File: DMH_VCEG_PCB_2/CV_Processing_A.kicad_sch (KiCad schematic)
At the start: 58 parts, among them J26 Conn_01x10_PinHeader, Q27 BC558, Q28 BC558, Q29 BC548, Q30 BC548, Q31 BC548, Q32 BC548, U18 TL074, U19 TL074, U20 TL074

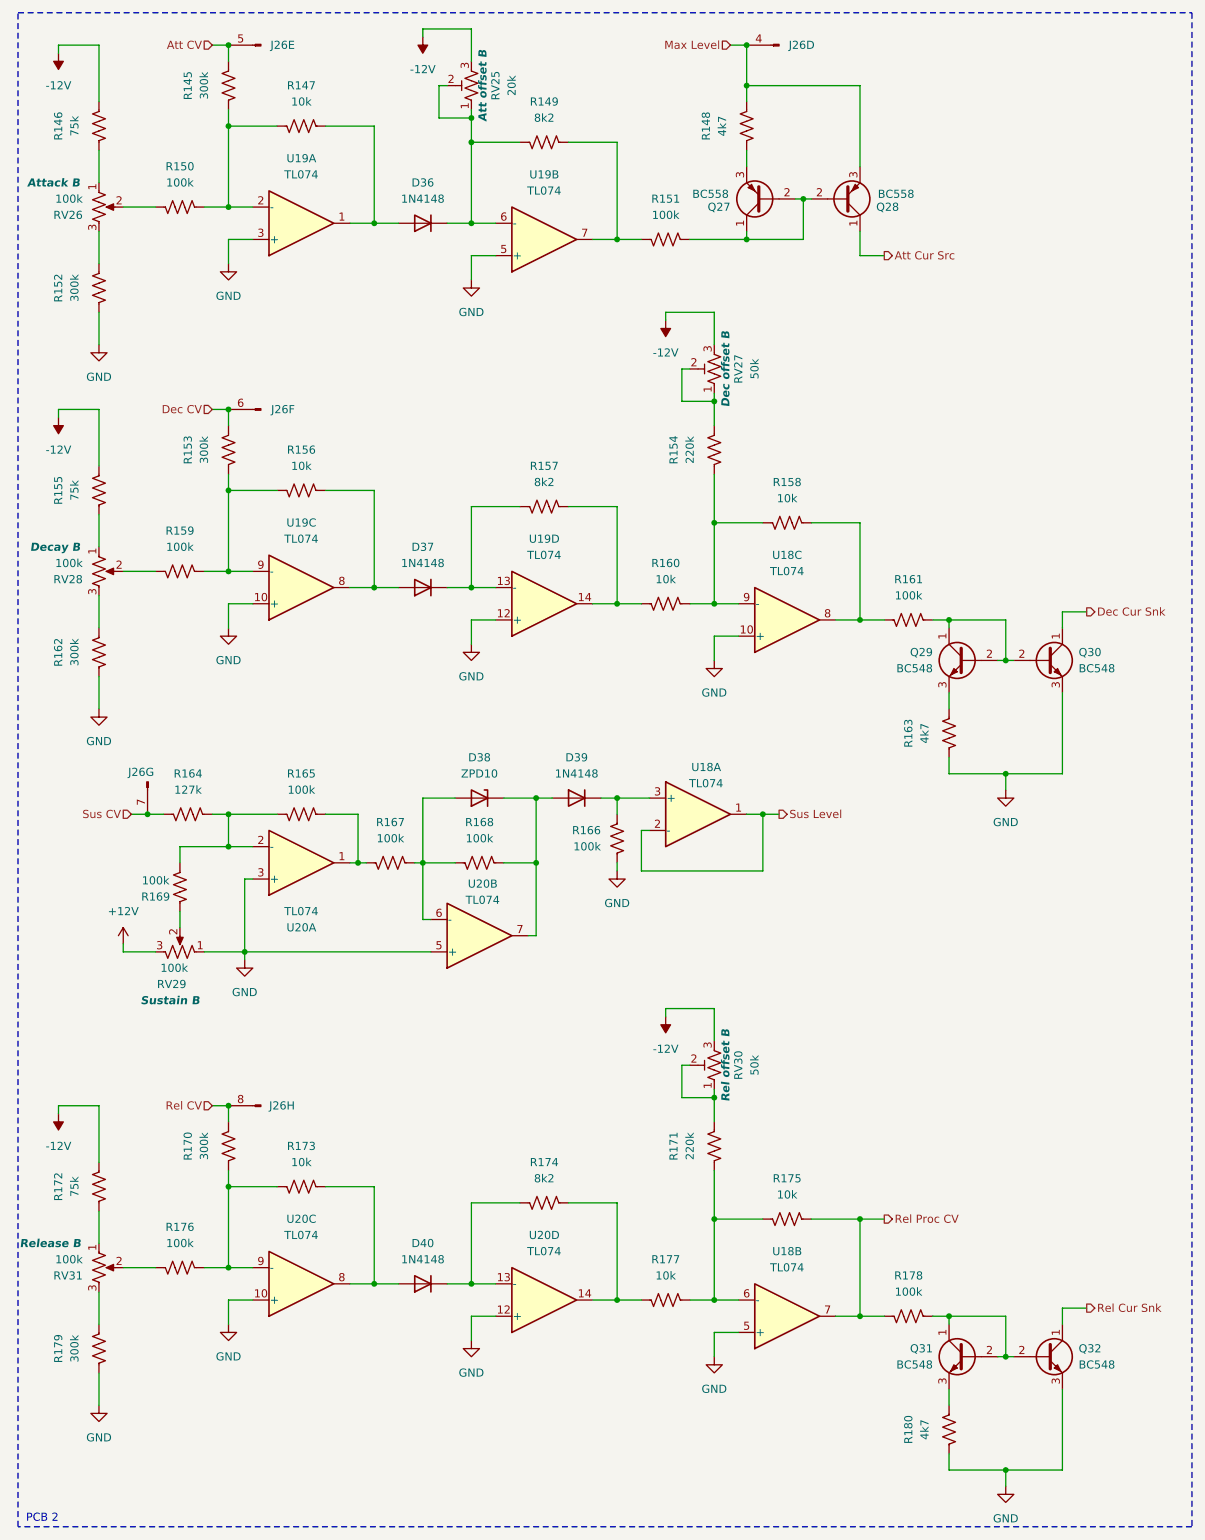
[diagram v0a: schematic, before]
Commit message: Synced PCB 2 project with PCB 1
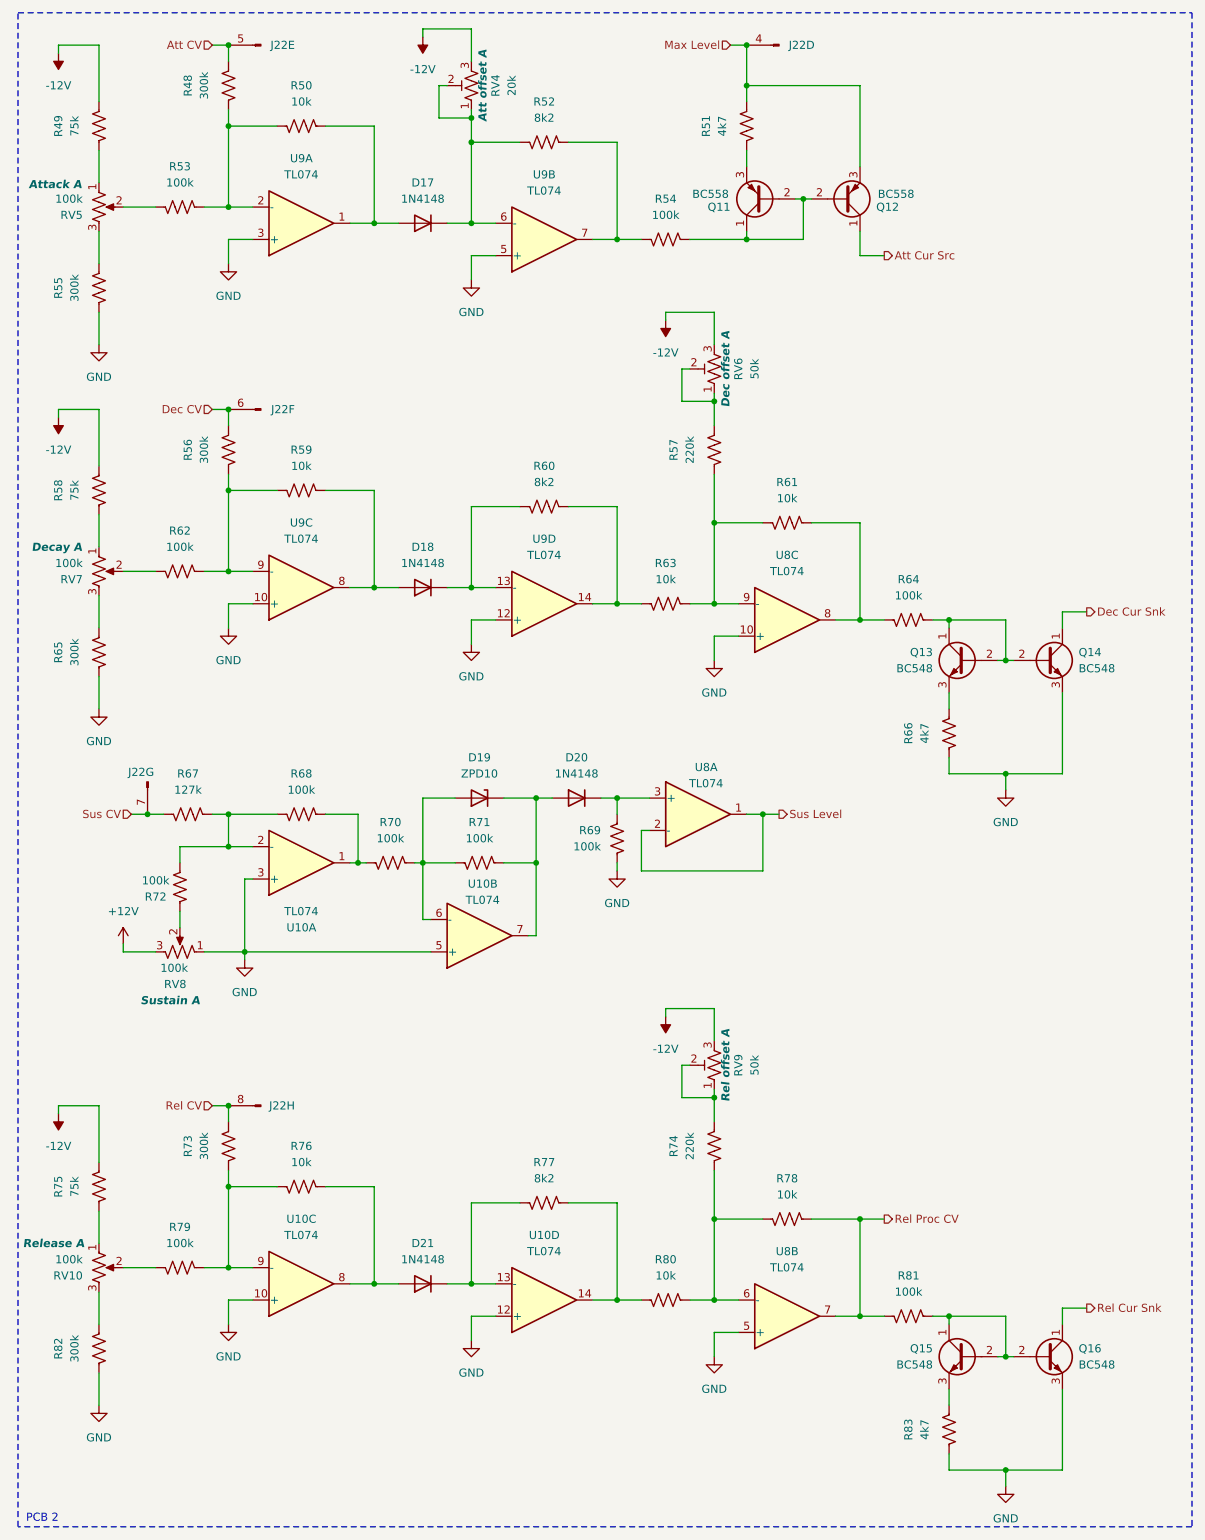
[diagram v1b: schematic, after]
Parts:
- removed D36, D37, D39, D40: 1N4148, Diode_THT:D_DO-35_SOD27_P7.62mm_Horizontal, symbol Diode:1N4148
- removed D38: ZPD10, Diode_THT:D_DO-35_SOD27_P7.62mm_Horizontal, symbol Diode:ZPDxx
- removed J26: Conn_01x10_PinHeader, Connector_PinHeader_2.54mm:PinHeader_1x10_P2.54mm_Vertical, symbol SynthStuff:Conn_01x10_PinHeader
- removed Q27, Q28: BC558, Package_TO_SOT_THT:TO-92L_Inline_Wide, symbol Transistor_BJT:BC558
- removed Q29, Q30, Q31, Q32: BC548, Package_TO_SOT_THT:TO-92L_Inline_Wide, symbol Transistor_BJT:BC548
- removed R145, R152, R153, R162, R170, R179: 300k, Resistor_THT:R_Axial_DIN0207_L6.3mm_D2.5mm_P7.62mm_Horizontal, symbol Device:R_US
- removed R146, R155, R172: 75k, Resistor_THT:R_Axial_DIN0207_L6.3mm_D2.5mm_P7.62mm_Horizontal, symbol Device:R_US
- removed R147, R156, R158, R160, R173, R175, R177: 10k, Resistor_THT:R_Axial_DIN0207_L6.3mm_D2.5mm_P7.62mm_Horizontal, symbol Device:R_US
- removed R148, R163, R180: 4k7, Resistor_THT:R_Axial_DIN0207_L6.3mm_D2.5mm_P7.62mm_Horizontal, symbol Device:R_US
- removed R149, R157, R174: 8k2, Resistor_THT:R_Axial_DIN0207_L6.3mm_D2.5mm_P7.62mm_Horizontal, symbol Device:R_US
- removed R150, R151, R159, R161, R165, R166, R167, R168, R169, R176, R178: 100k, Resistor_THT:R_Axial_DIN0207_L6.3mm_D2.5mm_P7.62mm_Horizontal, symbol Device:R_US
- removed R154, R171: 220k, Resistor_THT:R_Axial_DIN0207_L6.3mm_D2.5mm_P7.62mm_Horizontal, symbol Device:R_US
- removed R164: 127k, Resistor_THT:R_Axial_DIN0207_L6.3mm_D2.5mm_P7.62mm_Horizontal, symbol Device:R_US
- removed RV25: 20k, Potentiometer_THT:Potentiometer_Bourns_3296X_Horizontal, symbol Device:R_Potentiometer_Trim_US
- removed RV26, RV28, RV29, RV31: 100k, SynthStuff:Potentiometer_Alpha_RD901F-40-00D_Single_Vertical, symbol Device:R_Potentiometer_US
- removed RV27, RV30: 50k, Potentiometer_THT:Potentiometer_Bourns_3296X_Horizontal, symbol Device:R_Potentiometer_Trim_US
- removed U18, U19, U20: TL074, Package_DIP:DIP-14_W7.62mm_Socket, symbol Amplifier_Operational:TL074
- added D17, D18, D20, D21: 1N4148, Diode_THT:D_DO-35_SOD27_P7.62mm_Horizontal, symbol Diode:1N4148
- added D19: ZPD10, Diode_THT:D_DO-35_SOD27_P7.62mm_Horizontal, symbol Diode:ZPDxx
- added J22: Conn_01x10_PinHeader, Connector_PinSocket_2.54mm:PinSocket_1x10_P2.54mm_Vertical, symbol SynthStuff:Conn_01x10_PinHeader
- added Q11, Q12: BC558, Package_TO_SOT_THT:TO-92L_Inline_Wide, symbol Transistor_BJT:BC558
- added Q13, Q14, Q15, Q16: BC548, Package_TO_SOT_THT:TO-92L_Inline_Wide, symbol Transistor_BJT:BC548
- added R48, R55, R56, R65, R73, R82: 300k, Resistor_THT:R_Axial_DIN0207_L6.3mm_D2.5mm_P7.62mm_Horizontal, symbol Device:R_US
- added R49, R58, R75: 75k, Resistor_THT:R_Axial_DIN0207_L6.3mm_D2.5mm_P7.62mm_Horizontal, symbol Device:R_US
- added R50, R59, R61, R63, R76, R78, R80: 10k, Resistor_THT:R_Axial_DIN0207_L6.3mm_D2.5mm_P7.62mm_Horizontal, symbol Device:R_US
- added R51, R66, R83: 4k7, Resistor_THT:R_Axial_DIN0207_L6.3mm_D2.5mm_P7.62mm_Horizontal, symbol Device:R_US
- added R52, R60, R77: 8k2, Resistor_THT:R_Axial_DIN0207_L6.3mm_D2.5mm_P7.62mm_Horizontal, symbol Device:R_US
- added R53, R54, R62, R64, R68, R69, R70, R71, R72, R79, R81: 100k, Resistor_THT:R_Axial_DIN0207_L6.3mm_D2.5mm_P7.62mm_Horizontal, symbol Device:R_US
- added R57, R74: 220k, Resistor_THT:R_Axial_DIN0207_L6.3mm_D2.5mm_P7.62mm_Horizontal, symbol Device:R_US
- added R67: 127k, Resistor_THT:R_Axial_DIN0207_L6.3mm_D2.5mm_P7.62mm_Horizontal, symbol Device:R_US
- added RV10, RV5, RV7, RV8: 100k, SynthStuff:Potentiometer_Alpha_RD901F-40-00D_Single_Vertical, symbol Device:R_Potentiometer_US
- added RV4: 20k, Potentiometer_THT:Potentiometer_Bourns_3296X_Horizontal, symbol Device:R_Potentiometer_Trim_US
- added RV6, RV9: 50k, Potentiometer_THT:Potentiometer_Bourns_3296X_Horizontal, symbol Device:R_Potentiometer_Trim_US
- added U10, U8, U9: TL074, Package_DIP:DIP-14_W7.62mm_Socket, symbol Amplifier_Operational:TL074
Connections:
- net +12V: now also RV8.3
- net -12V: now also R49.2, R58.2, R75.2, RV4.3, RV6.3, RV9.3
- net Att CV: now also J22.5 (Pin_5), R48.2
- net Att Cur Src: now also Q12.1 (C)
- net Dec CV: now also J22.6 (Pin_6), R56.2
- net Dec Cur Snk: now also Q14.1 (C)
- net GND: now also Q14.3 (E), Q16.3 (E), R55.1, R65.1, R66.1, R69.1, R82.1, R83.1, RV8.1, U10.10 (+), U10.12 (+), U10.3 (+), U10.5 (+), U8.10 (+), U8.5 (+), U9.10 (+), U9.12 (+), U9.3 (+), U9.5 (+)
- net Max Level: now also J22.4 (Pin_4), Q12.3 (E), R51.2
- net Rel CV: now also J22.8 (Pin_8), R73.2
- net Rel Cur Snk: now also Q16.1 (C)
- net Rel Proc CV: now also R78.2, R81.1, U8.7
- net Sus CV: now also J22.7 (Pin_7), R67.1
- net Sus Level: now also U8.1, U8.2 (-)
- new net: D20.1 (K), R69.2, U8.3 (+)
- new net: R57.1, R61.1, R63.2, U8.9 (-)
- new net: R61.2, R64.1, U8.8
- new net: R67.2, R68.1, R72.2, U10.2 (-)
- new net: R68.2, R70.1, U10.1
- new net: D18.2 (A), R59.2, U9.8
- new net: R56.1, R59.1, R62.2, U9.9 (-)
- new net: R49.1, RV5.1
- new net: R53.1, RV5.2
- new net: R55.2, RV5.3
- new net: R82.2, RV10.3
- new net: D19.2 (A), R70.2, R71.1, U10.6 (-)
- new net: Q15.3 (E), R83.2
- new net: R74.2, RV9.1, RV9.2
- new net: D18.1 (K), R60.1, U9.13 (-)
- new net: Q15.1 (C), Q15.2 (B), Q16.2 (B), R81.2
- new net: R58.1, RV7.1
- new net: D19.1 (K), D20.2 (A), R71.2, U10.7
- new net: R57.2, RV6.1, RV6.2
- new net: R60.2, R63.1, U9.14
- new net: Q11.1 (C), Q11.2 (B), Q12.2 (B), R54.2
- new net: Q11.3 (E), R51.1
- new net: D21.1 (K), R77.1, U10.13 (-)
- new net: D21.2 (A), R76.2, U10.8
- new net: D17.1 (K), R52.1, RV4.1, RV4.2, U9.6 (-)
- new net: R79.1, RV10.2
- new net: R73.1, R76.1, R79.2, U10.9 (-)
- new net: Q13.3 (E), R66.2
- new net: R48.1, R50.1, R53.2, U9.2 (-)
- new net: R52.2, R54.1, U9.7
- new net: D17.2 (A), R50.2, U9.1
- new net: R65.2, RV7.3
- new net: R75.1, RV10.1
- new net: R74.1, R78.1, R80.2, U8.6 (-)
- new net: R72.1, RV8.2
- new net: R77.2, R80.1, U10.14
- new net: R62.1, RV7.2
- new net: Q13.1 (C), Q13.2 (B), Q14.2 (B), R64.2

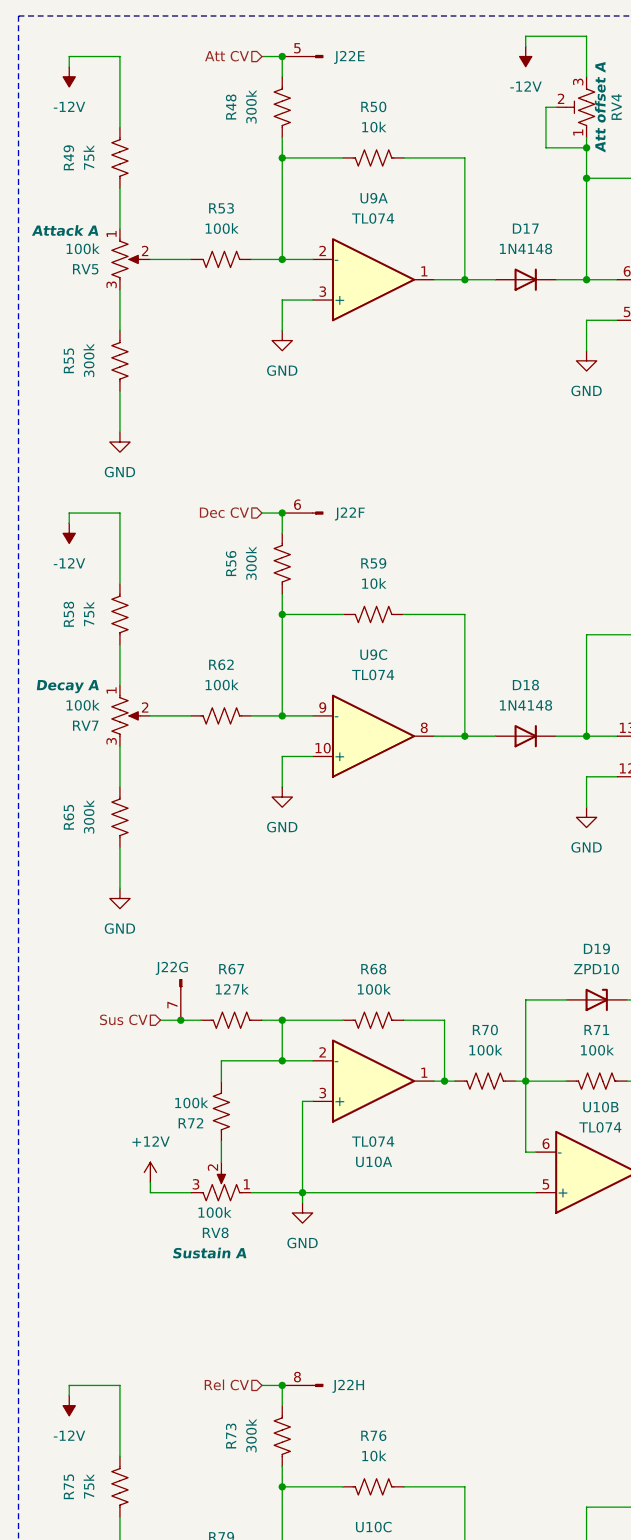
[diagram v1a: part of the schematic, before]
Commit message: PCB 2 placement in progress
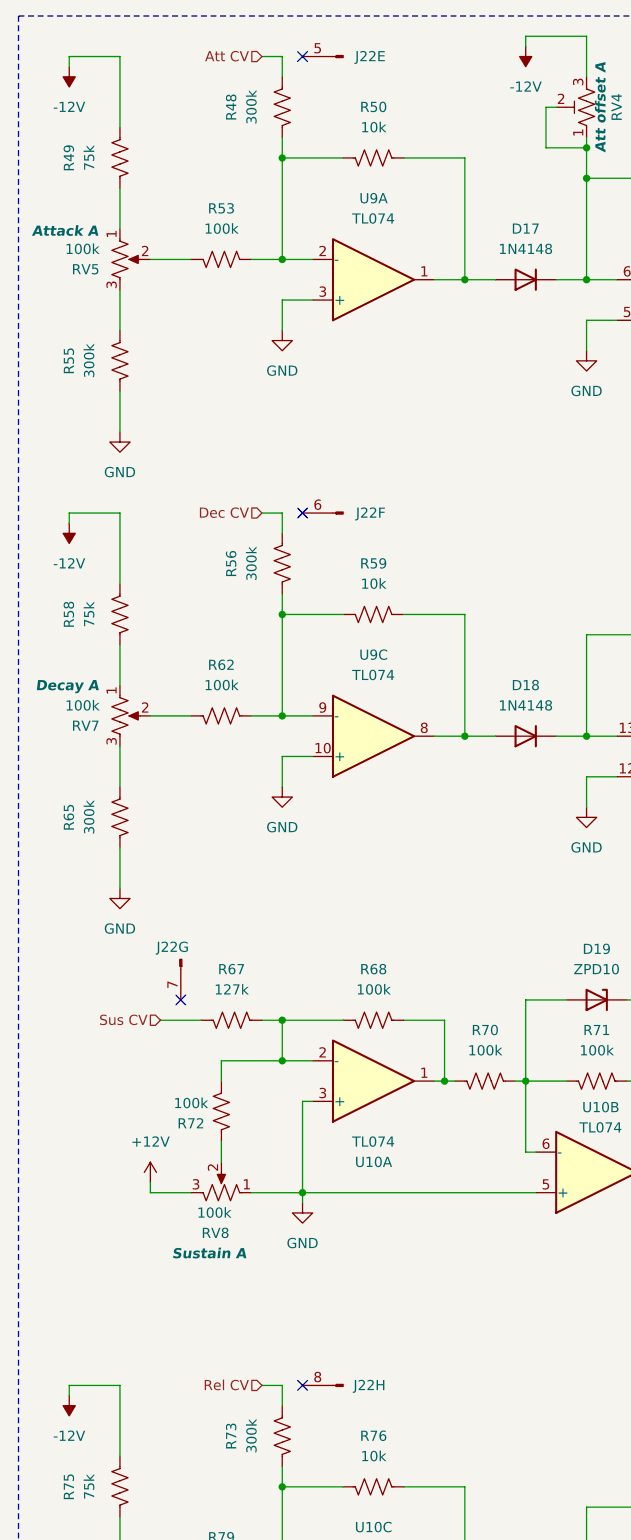
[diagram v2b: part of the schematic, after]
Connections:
- net Att CV: no longer J22.5 (Pin_5)
- net Dec CV: no longer J22.6 (Pin_6)
- net Rel CV: no longer J22.8 (Pin_8)
- net Sus CV: no longer J22.7 (Pin_7)
- no-connect marks 0 -> 4

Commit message: Updated Dec and Rel trimpots to 100k
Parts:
- RV6, RV9: value 50k -> 100k
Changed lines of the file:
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@@
 			)
 		)
-		(property "Value" "50k"
+		(property "Value" "100k"
 			(at 128.27 179.07 90)
 			(effects
@@
 			)
 		)
-		(property "Value" "50k"
+		(property "Value" "100k"
 			(at 128.27 69.85 90)
 			(effects

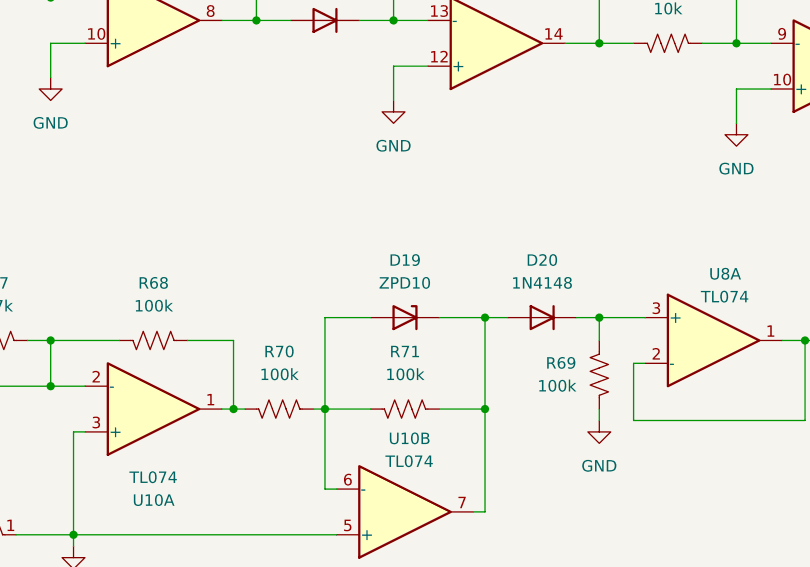
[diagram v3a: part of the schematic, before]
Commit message: PCB 2 placement ongoing
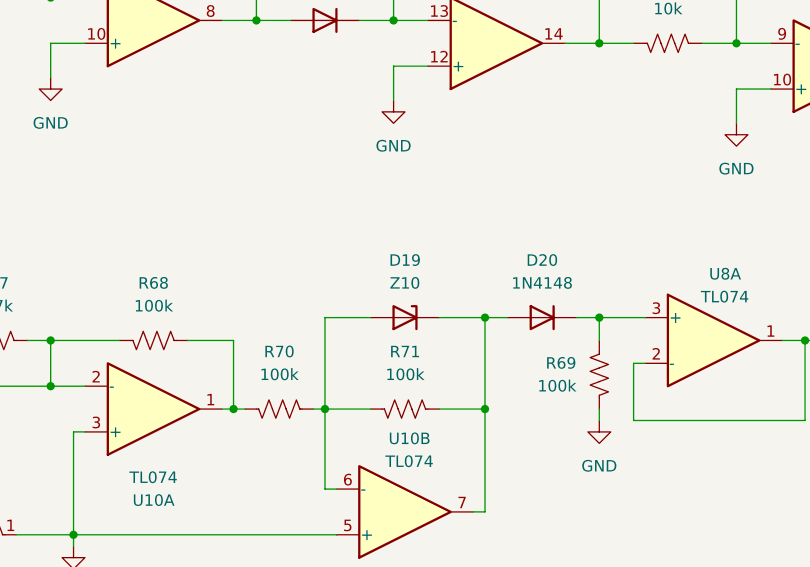
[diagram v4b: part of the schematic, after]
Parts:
- D19: value ZPD10 -> Z10
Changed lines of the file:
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@@
 			)
 		)
-		(property "Value" "ZPD10"
+		(property "Value" "Z10"
 			(at 85.09 133.35 0)
 			(effects
@@
 			)
 		)
+		(property "Function" ""
+			(at 85.09 137.16 0)
+			(effects
+				(font
+					(size 1.27 1.27)
+				)
+			)
+		)

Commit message: PCB 2 routing in progress
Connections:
- net Att CV: now also J22.5 (Pin_5)
- net Dec CV: now also J22.6 (Pin_6)
- net Rel CV: now also J22.8 (Pin_8)
- net Sus CV: now also J22.7 (Pin_7)
- no-connect marks 4 -> 0
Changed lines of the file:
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@@
+	)
+	(junction
+		(at 33.02 139.7)
+		(diameter 0)
+		(color 0 0 0 0)
 	)
 	(junction
@@
 	)
 	(junction
+		(at 45.72 76.2)
+		(diameter 0)
+		(color 0 0 0 0)
+	)
+	(junction
 		(at 135.89 43.18)
 		(diameter 0)
@@
 	)
 	(junction
+		(at 45.72 19.05)
+		(diameter 0)
+		(color 0 0 0 0)
+	)
+	(junction
 		(at 121.92 74.93)
 		(diameter 0)
@@
 	)
 	(junction
+		(at 45.72 185.42)
+		(diameter 0)
+		(color 0 0 0 0)
+	)
+	(junction
 		(at 106.68 106.68)
 		(diameter 0)
@@
 		(color 0 0 0 0)
 	)
-	(no_connect
-		(at 48.26 19.05)
-	)
-	(no_connect
-		(at 48.26 76.2)
-	)
-	(no_connect
-		(at 33.02 137.16)
-	)
-	(no_connect
-		(at 48.26 185.42)
-	)
 	(wire
 		(pts
@@
 	(wire
 		(pts
+			(xy 45.72 185.42) (xy 48.26 185.42)
+		)
+		(stroke
+			(width 0)
+			(type default)
+		)
+	)
+	(wire
+		(pts
 			(xy 167.64 115.57) (xy 168.91 115.57)
 		)
@@
 	(wire
 		(pts
+			(xy 45.72 76.2) (xy 48.26 76.2)
+		)
+		(stroke
+			(width 0)
+			(type default)
+		)
+	)
+	(wire
+		(pts
 			(xy 158.75 133.35) (xy 167.64 133.35)
 		)
@@
 	(wire
 		(pts
+			(xy 33.02 137.16) (xy 33.02 139.7)
+		)
+		(stroke
+			(width 0)
+			(type default)
+		)
+	)
+	(wire
+		(pts
 			(xy 45.72 76.2) (xy 45.72 78.74)
 		)
@@
 	(wire
 		(pts
+			(xy 48.26 19.05) (xy 45.72 19.05)
+		)
+		(stroke
+			(width 0)
+			(type default)
+		)
+	)
+	(wire
+		(pts
 			(xy 25.4 76.2) (xy 25.4 85.09)
 		)
@@
 	(wire
 		(pts
+			(xy 33.02 139.7) (xy 35.56 139.7)
+		)
+		(stroke
+			(width 0)
+			(type default)
+		)
+	)
+	(wire
+		(pts
 			(xy 167.64 109.22) (xy 167.64 115.57)
 		)
@@
 	(wire
 		(pts
-			(xy 30.48 139.7) (xy 35.56 139.7)
-		)
-		(stroke
+			(xy 30.48 139.7) (xy 33.02 139.7)
+		)
+		(stroke
